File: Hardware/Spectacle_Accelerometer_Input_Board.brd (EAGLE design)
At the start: 25.4 x 55.9 mm, 38 parts, among them J19 FTDI_DEVICE, U1 CY8C4146LQI-S422, U2 3.3V/150mA, U3 ADXL345

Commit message: Review feedback
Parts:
- added FD1, FD2: FIDUCIALUFIDUCIAL, SparkFun-Aesthetics:MICRO-FIDUCIAL
- added LOGO3: OSHW-LOGOS, SparkFun-Aesthetics:OSHW-LOGO-S
- added LOGO4: SFE_LOGO_NAME_FLAME.1_INCH, SparkFun-Aesthetics:SFE_LOGO_NAME_FLAME_.1
- added U$3: (no value), SparkFun-Aesthetics:SPECTACLE_LOGO_TITLE_0.35X0.70
- added U$4: (no value), SparkFun-Aesthetics:SPECTACLE_LOGO_NEGATIVE_2.2X1.0
- moved R7 0.51 mm to (8.13, 46.2)
- moved U3 0.51 mm to (12.7, 46.2)
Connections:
- new net N$1: U1.1
- new net N$10: U1.3
- new net N$12: U1.4
- new net N$13: U1.5
- new net N$14: U1.6
- new net N$15: U1.7
- new net N$16: U1.10
- new net N$17: U1.9
- new net N$18: U1.14
- new net N$19: U1.15
- new net N$20: U1.16
- new net N$7: U1.32
- new net N$8: U1.31
- new net N$9: U1.2
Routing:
- net GND: track 11.8 -> 12.8 mm
- net N$33: track 0.00 -> 0.90 mm
- net N$32: track 0.00 -> 0.76 mm
- net N$31: track 0.00 -> 0.63 mm
- net N$29: track 0.00 -> 0.60 mm
- net N$27: track 0.00 -> 0.58 mm
- net N$9: track 0.00 -> 0.57 mm
- net N$25: track 0.00 -> 0.57 mm
- net N$15: track 0.00 -> 0.57 mm
- net N$13: track 0.00 -> 0.57 mm
- net N$10: track 0.00 -> 0.57 mm
- net N$28: track 0.00 -> 0.56 mm
- net N$24: track 0.00 -> 0.56 mm
- net N$22: track 0.00 -> 0.56 mm
- net N$21: track 0.00 -> 0.56 mm
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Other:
- board text added: "Accelerometer"
- board text removed: "Spectacle\! Accelerometer Input Board"

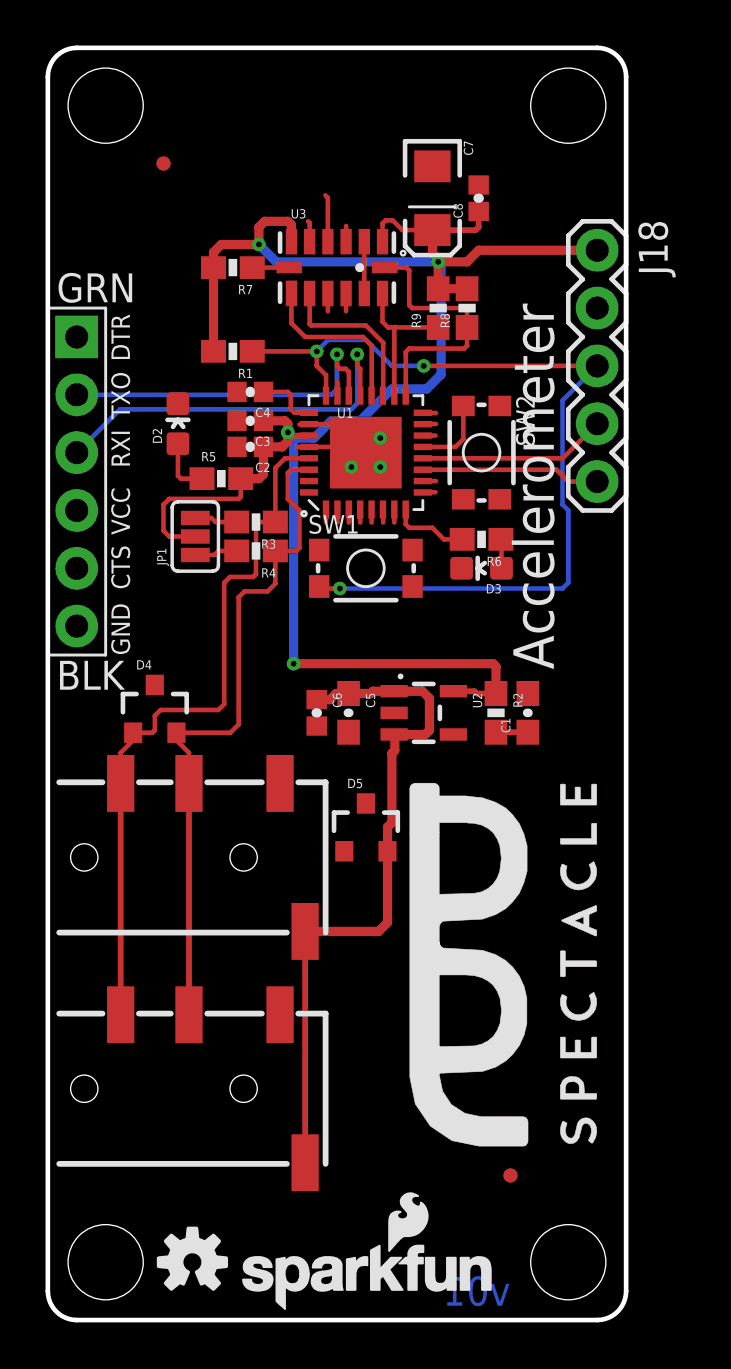
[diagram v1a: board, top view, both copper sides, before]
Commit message: Fixed issues from Eric's review
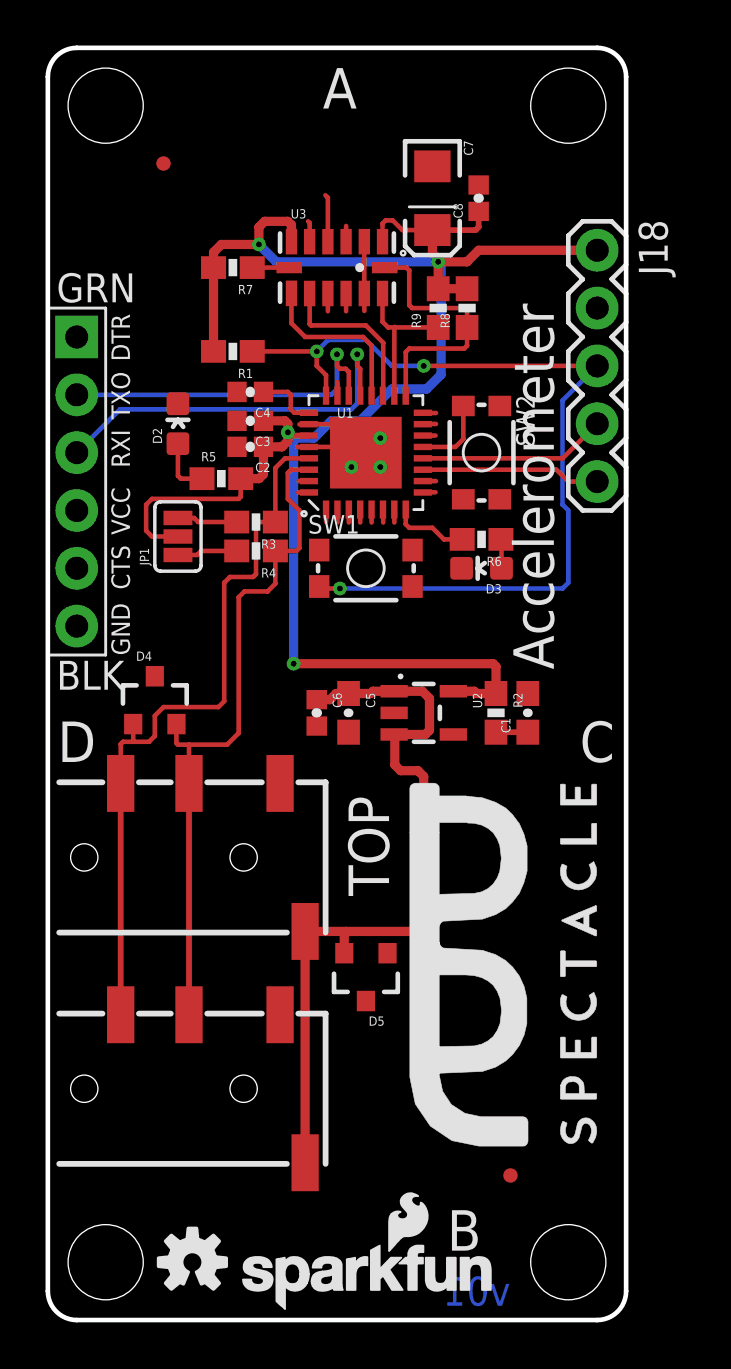
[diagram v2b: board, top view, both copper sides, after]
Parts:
- D3: value RED -> Yellow
- moved D5 6.48 mm to (14.0, 15.1), turned to 180 degrees
- moved JP1 0.76 mm to (5.71, 34.4)
- moved D4 0.38 mm to (4.70, 27.2)
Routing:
- net VIN: track 30.6 -> 34.0 mm
- net SCL: track 31.5 -> 32.4 mm
- net N$6: track 1.89 -> 2.65 mm
- net 3.3V: track 83.1 -> 83.9 mm
- net N$2: track 1.89 -> 2.65 mm
- net N$36: track 0.00 -> 0.63 mm
- net SDA: track 30.1 -> 30.7 mm
- net N$35: track 0.00 -> 0.50 mm
- net N$34: track 0.00 -> 0.50 mm
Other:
- board text added: "A"
- board text added: "B"
- board text added: "BOTTOM"
- board text added: "C"
- board text added: "D"
- board text added: "TOP"

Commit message: Added downstream power control circuitry
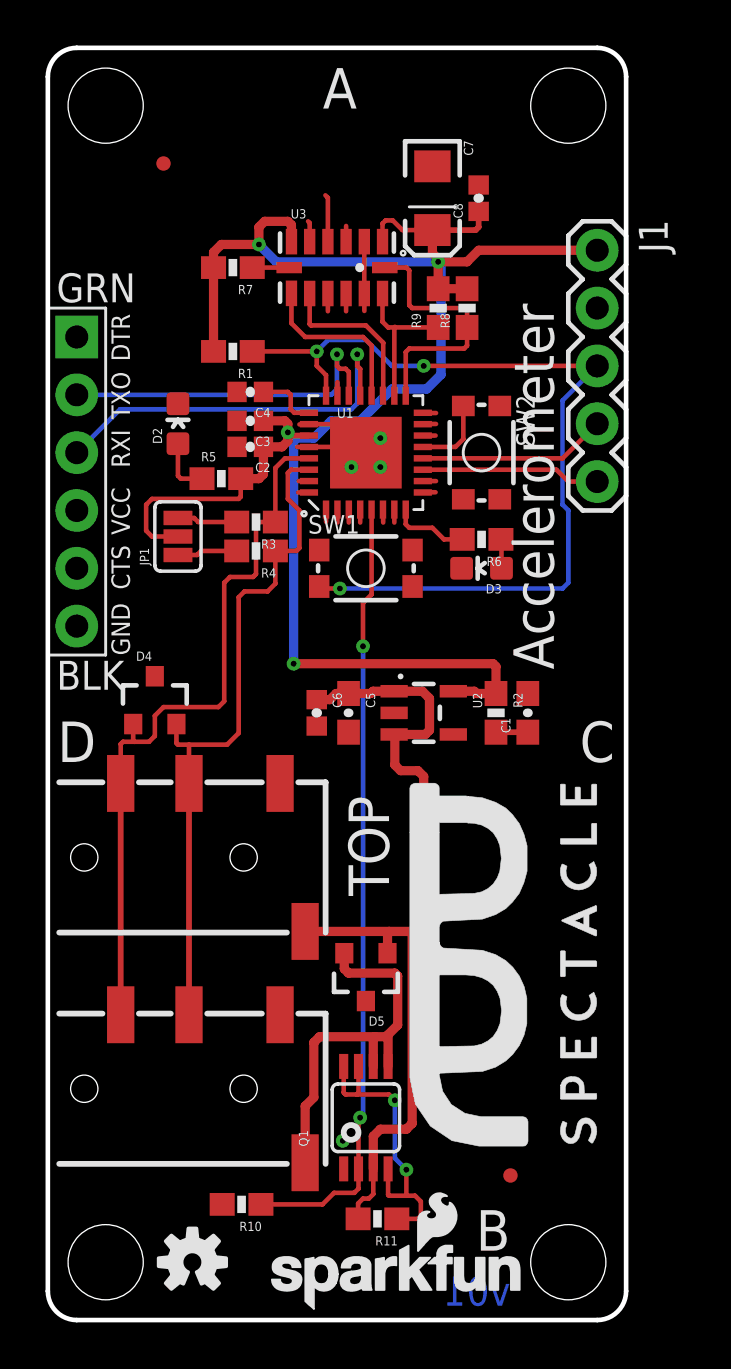
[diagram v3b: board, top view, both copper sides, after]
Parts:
- added Q1: (no value), SparkFun-DiscreteSemi:MSOP8
- added R10, R11: 10K, SparkFun-Resistors:0603-RES
- moved LOGO1 1.27 mm to (9.40, 0.38)
- renumbered J18 to J1, J19 to J2, U$1 to J3, U$2 to J4
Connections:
- removed net N$13: U1.5
- new net N$37: Q1.4, Q1.7, Q1.8, R11.1
- new net VOUT: D5.2, J4.EARTH, Q1.5, Q1.6
- new net V_OUT_EN: Q1.2, R10.1, U1.5
- net GND: now also Q1.1, R10.2
- net VIN: now also D5.1, Q1.3, R11.2; no longer D5.2, J4.EARTH
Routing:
- net V_OUT_EN: track 0.00 -> 34.6 mm, vias 0 -> 2
- net VOUT: track 0.00 -> 17.5 mm
- net N$37: track 0.00 -> 13.6 mm, vias 0 -> 2
- net VIN: track 34.0 -> 38.3 mm
- net N$13: track 0.57 -> 0.00 mm
- net GND: vias 3 -> 4

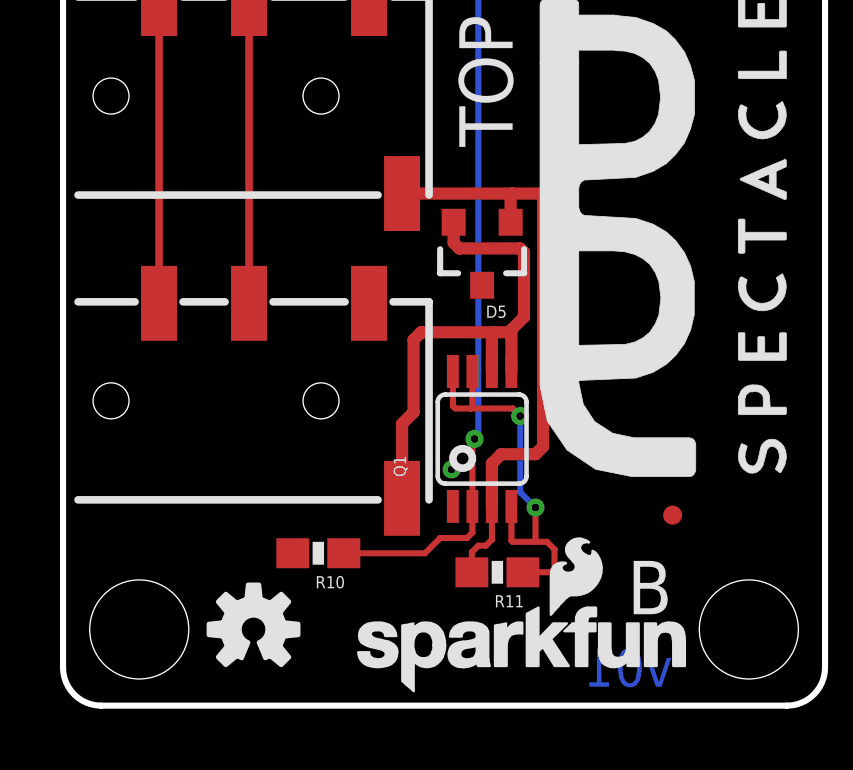
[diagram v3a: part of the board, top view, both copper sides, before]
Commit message: Added notes to IN and OUT connectors
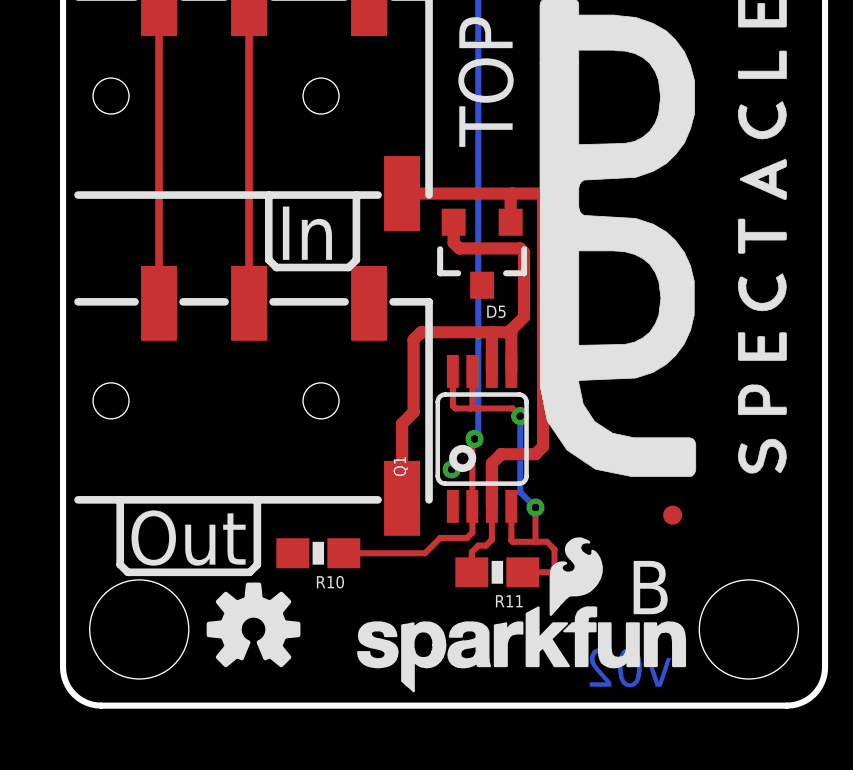
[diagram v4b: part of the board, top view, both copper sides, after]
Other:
- board text added: "In"
- board text added: "Out"
- board text added: "v02"
- board text removed: "v01"
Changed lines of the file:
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@@
 <text x="33.147" y="72.898" size="1.778" layer="47" ratio="15">(typ.)</text>
 <dimension x1="0" y1="0" x2="0" y2="20.32" x3="-12.7" y3="10.16" textsize="1.778" textratio="15" layer="47" dtype="vertical" unit="inch"/>
-<text x="20.32" y="0.635" size="1.27" layer="16" font="vector" ratio="15" rot="MR0">v01</text>
+<text x="20.32" y="0.635" size="1.27" layer="16" font="vector" ratio="15" rot="MR0">v02</text>
 <dimension x1="0" y1="0" x2="0" y2="10.16" x3="-8.89" y3="5.08" textsize="1.778" textratio="15" layer="47" dtype="vertical" unit="inch"/>
 <text x="22.225" y="28.575" size="1.778" layer="21" font="vector" ratio="15" rot="R90">Accelerometer</text>
@@
 <text x="14.097" y="20.828" size="1.778" layer="21" font="vector" ratio="15" rot="R90" align="center">TOP</text>
 <text x="4.445" y="32.512" size="1.778" layer="22" font="vector" ratio="15" rot="MR90" align="center">BOTTOM</text>
+<text x="7.112" y="14.859" size="1.778" layer="21" font="vector" ratio="15">In</text>
+<text x="2.159" y="4.699" size="1.778" layer="21" font="vector" ratio="15">Out</text>
+<wire x1="1.905" y1="6.858" x2="1.905" y2="4.699" width="0.254" layer="21"/>
+<wire x1="1.905" y1="4.699" x2="2.159" y2="4.445" width="0.254" layer="21"/>
+<wire x1="2.159" y1="4.445" x2="6.223" y2="4.445" width="0.254" layer="21"/>
+<wire x1="6.223" y1="4.445" x2="6.477" y2="4.699" width="0.254" layer="21"/>
+<wire x1="6.477" y1="4.699" x2="6.477" y2="6.858" width="0.254" layer="21"/>
+<wire x1="6.858" y1="17.018" x2="6.858" y2="14.859" width="0.254" layer="21"/>
+<wire x1="6.858" y1="14.859" x2="7.112" y2="14.605" width="0.254" layer="21"/>
+<wire x1="7.112" y1="14.605" x2="9.525" y2="14.605" width="0.254" layer="21"/>
+<wire x1="9.525" y1="14.605" x2="9.779" y2="14.859" width="0.254" layer="21"/>
+<wire x1="9.779" y1="14.859" x2="9.779" y2="17.018" width="0.254" layer="21"/>
 </plain>
 <attributes>

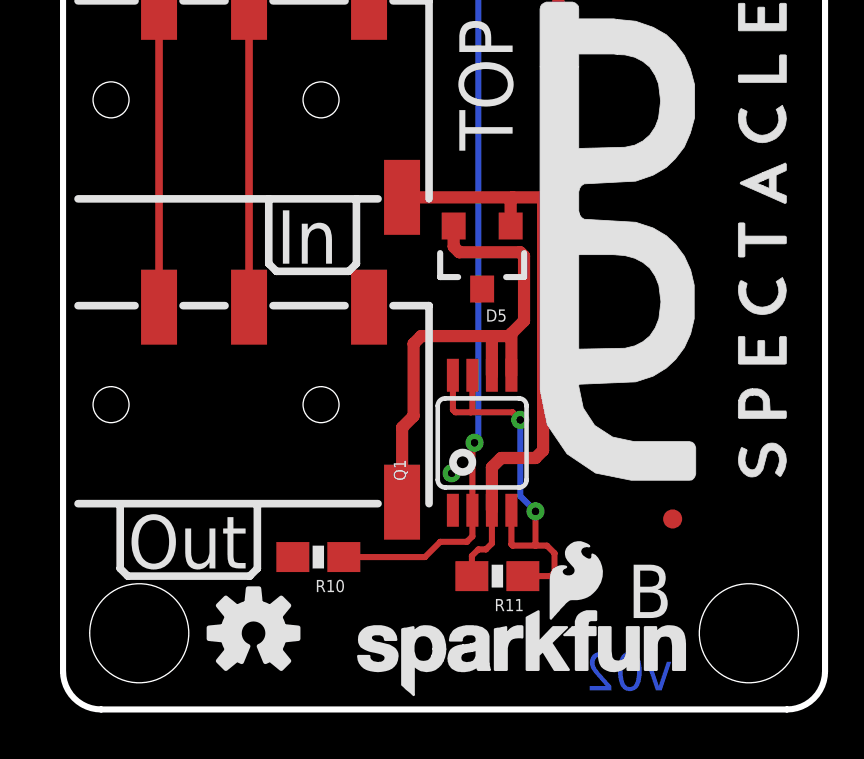
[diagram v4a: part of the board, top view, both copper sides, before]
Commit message: Fixes from design review
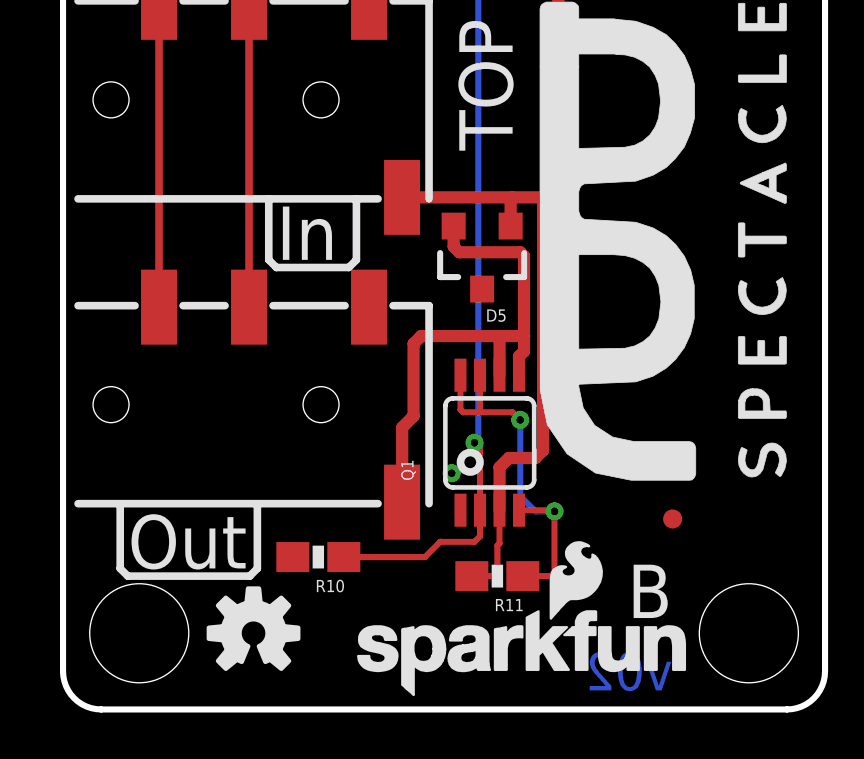
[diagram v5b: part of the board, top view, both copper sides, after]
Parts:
- moved Q1 0.25 mm to (14.2, 8.89)
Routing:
- net N$37: track 13.6 -> 12.8 mm
